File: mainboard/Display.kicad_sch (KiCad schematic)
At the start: 4 parts, among them X1401 DISPLAY

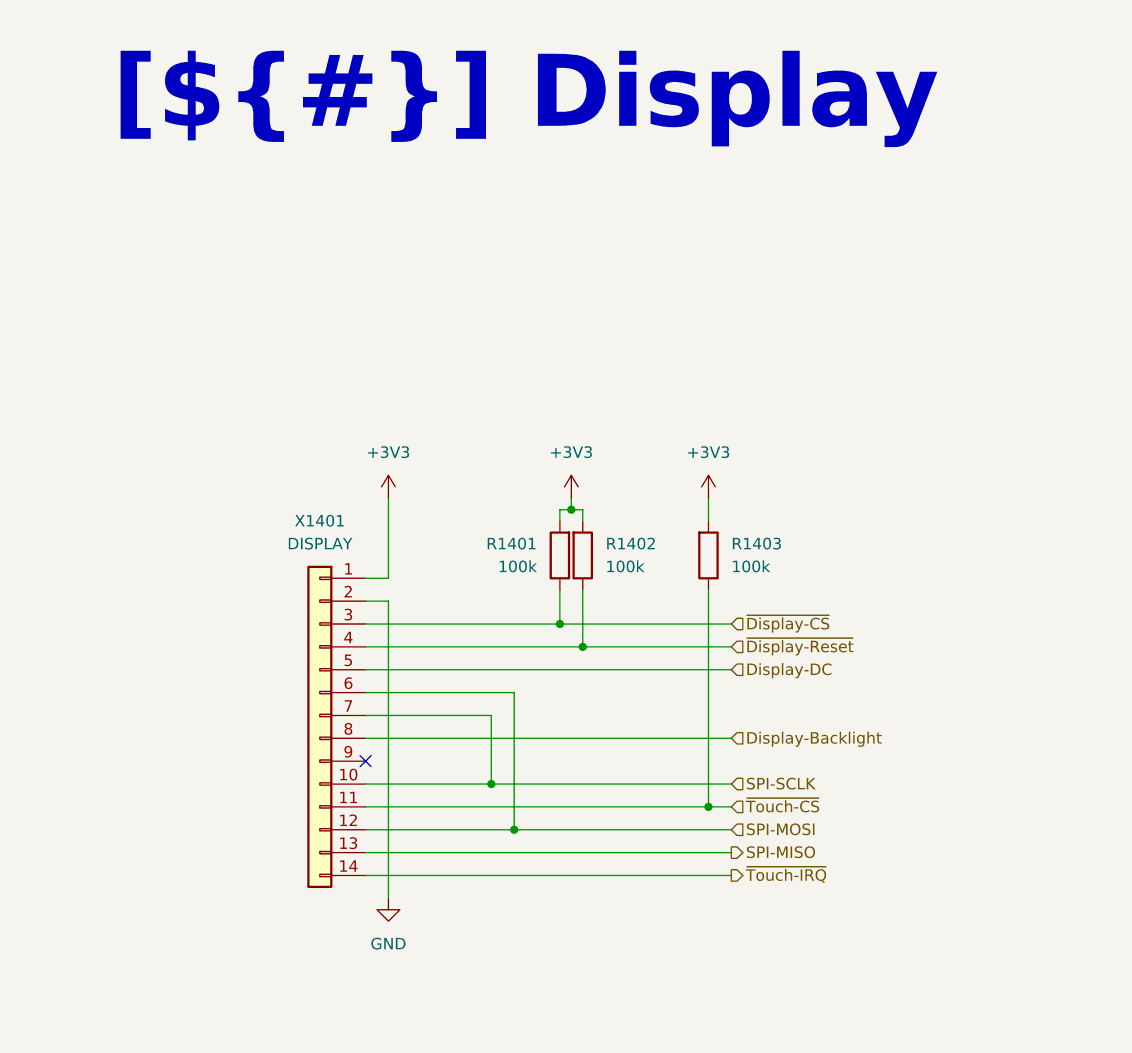
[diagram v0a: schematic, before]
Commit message: Continue routing, add flash LEDs for the RGB camera, add PWM controller for the Display Backlight and the flash LEDs, add Polyfuse for the battery
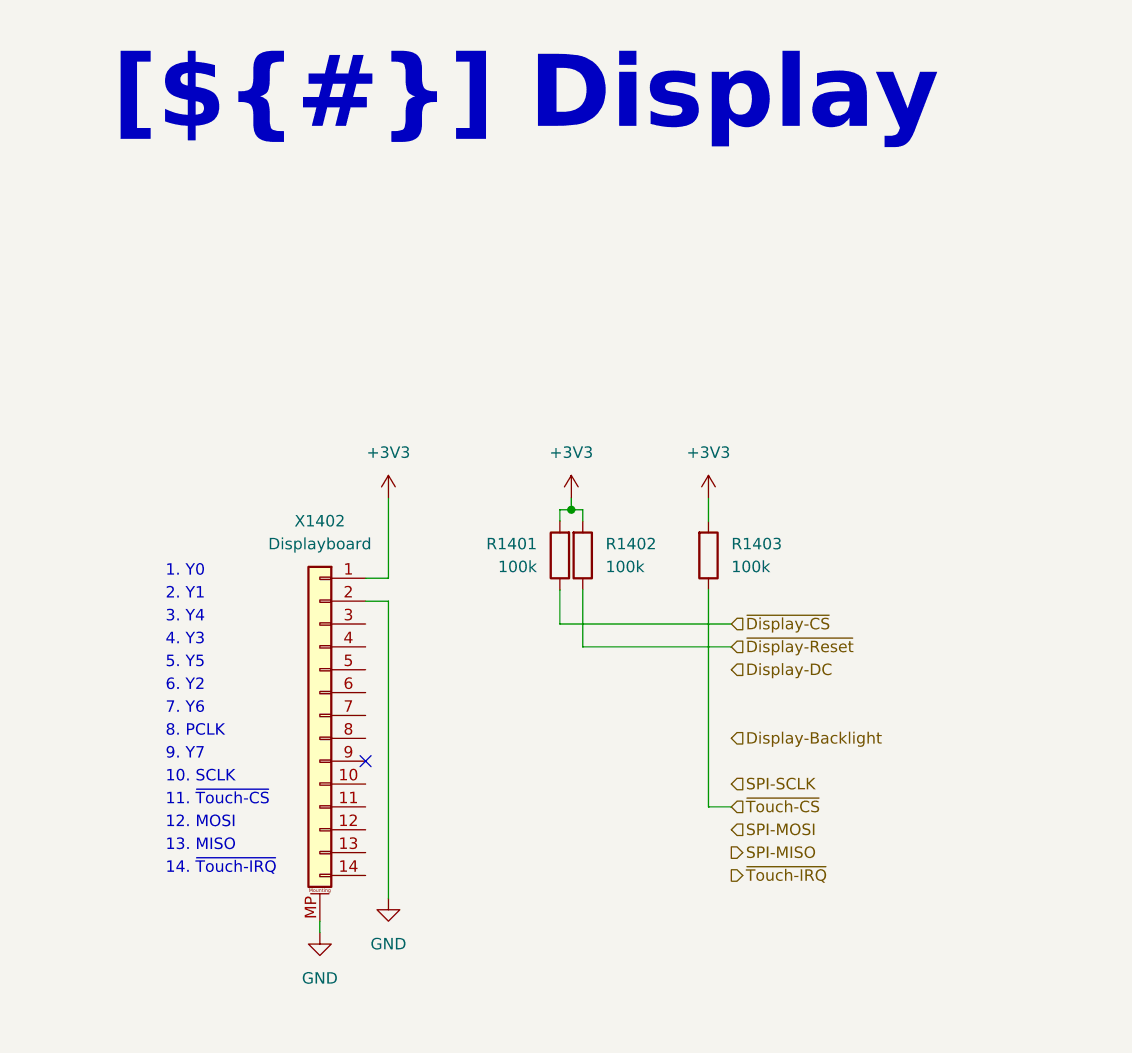
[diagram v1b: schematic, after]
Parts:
- removed X1401: DISPLAY, Connector_PinSocket_2.54mm:PinSocket_1x14_P2.54mm_Vertical, symbol Connector_Generic:Conn_01x14
- added X1402: Displayboard, Connector_FFC-FPC:Amphenol_F32R-1A7x1-11014_1x14-1MP_P0.5mm_Horizontal, symbol Connector_Generic_MountingPin:Conn_01x14_MountingPin
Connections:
- net +3V3: now also X1402.1 (Pin_1)
- net GND: now also X1402.2 (Pin_2), X1402.MP (MountPin)
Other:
- note added: "1. Y0"
- note added: "10. SCLK"
- note added: "11. ~{Touch-CS}"
- note added: "12. MOSI"
- note added: "13. MISO"
- note added: "14. ~{Touch-IRQ}"
- note added: "2. Y1"
- note added: "3. Y4"
- note added: "4. Y3"
- note added: "5. Y5"
- note added: "6. Y2"
- note added: "7. Y6"
- note added: "8. PCLK"
- note added: "9. Y7"

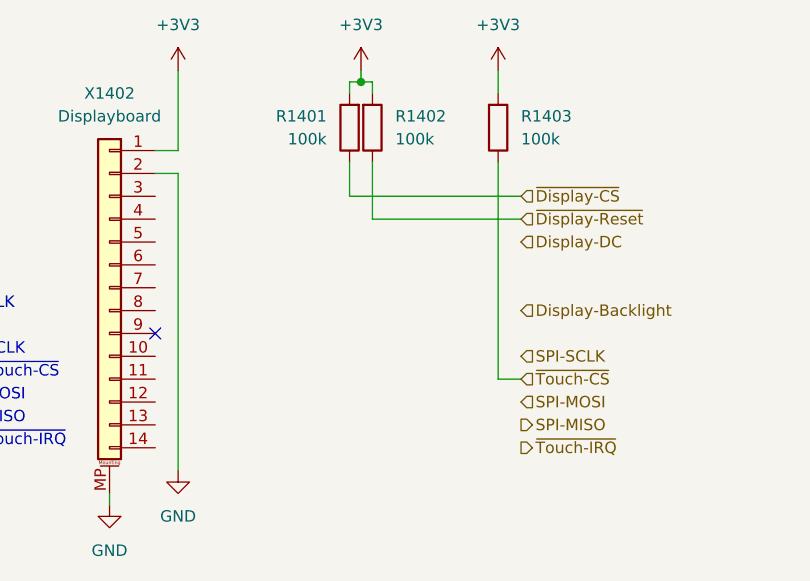
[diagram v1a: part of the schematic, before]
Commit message: New position for display connector
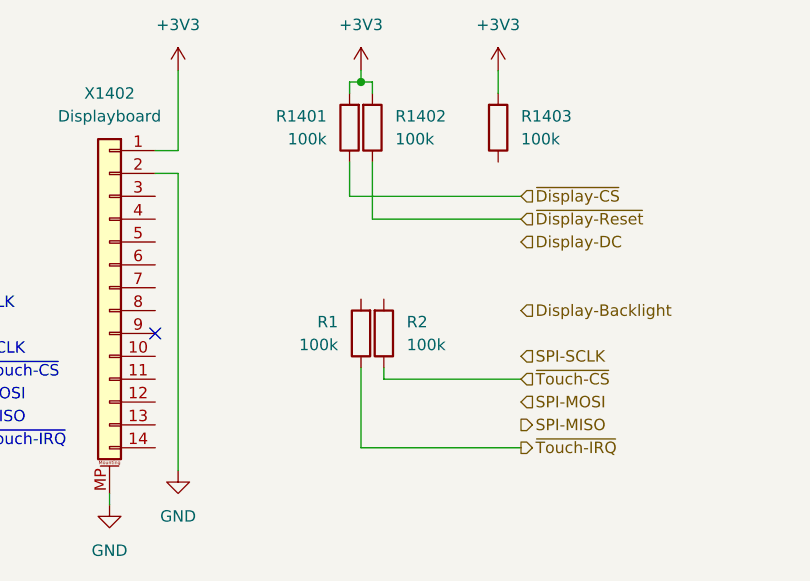
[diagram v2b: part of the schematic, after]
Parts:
- added R1, R2: 100k, Resistor_SMD:R_0603_1608Metric, symbol Device:R
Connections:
- net ~{Touch-CS}: now also R2.1; no longer R1403.1
- net ~{Touch-IRQ}: now also R1.1
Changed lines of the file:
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@@
+	(wire
+		(pts
+			(xy 156.21 99.06) (xy 156.21 97.79)
+		)
+		(stroke
+			(width 0)
+			(type default)
+		)
+	)
 	(wire
 		(pts
@@
 	(wire
 		(pts
+			(xy 171.45 106.68) (xy 153.67 106.68)
+		)
+		(stroke
+			(width 0)
+			(type default)
+		)
+	)
+	(wire
+		(pts
 			(xy 154.94 81.28) (xy 171.45 81.28)
 		)
@@
 	(wire
 		(pts
-			(xy 168.91 99.06) (xy 171.45 99.06)
+			(xy 153.67 106.68) (xy 153.67 97.79)
+		)
+		(stroke
+			(width 0)
+			(type default)
+		)
+	)
+	(wire
+		(pts
+			(xy 156.21 99.06) (xy 171.45 99.06)
 		)
 		(stroke
@@
 		(pts
 			(xy 133.35 76.2) (xy 133.35 109.22)
-		)
-		(stroke
-			(width 0)
-			(type default)
-		)
-	)
-	(wire
-		(pts
-			(xy 168.91 74.93) (xy 168.91 99.06)
 		)
 		(stroke
@@
 	)
 	(symbol
+		(lib_id "Device:R")
+		(at 153.67 93.98 180)
+		(unit 1)
+		(exclude_from_sim no)
+		(in_bom yes)
+		(on_board yes)
+		(dnp no)
+		(property "Reference" "R1"
+			(at 151.13 92.7099 0)
+			(effects
+				(font
+					(size 1.27 1.27)
+				)
+				(justify left)
+			)
+		)
+		(property "Value" "100k"
+			(at 151.13 95.2499 0)
+			(effects
+				(font
+					(size 1.27 1.27)
+				)
+				(justify left)
+			)
+		)
+		(property "Footprint" "Resistor_SMD:R_0603_1608Metric"
+			(at 155.448 93.98 90)
+			(effects
+				(font
+					(size 1.27 1.27)
+				)
+				(hide yes)
+			)
+		)
+		(property "Datasheet" "https://www.mouser.de/datasheet/2/54/cr-1858361.pdf"
+			(at 153.67 93.98 0)
+			(effects
+				(font
+					(size 1.27 1.27)
+				)
+				(hide yes)
+			)
+		)
+		(property "Description" "Resistor"
+			(at 153.67 93.98 0)
+			(effects
+				(font
+					(size 1.27 1.27)
+				)
+				(hide yes)
+			)
+		)
+		(property "CONFIG" ""
+			(at 153.67 93.98 0)
+			(effects
+				(font
+					(size 1.27 1.27)
+				)
+				(hide yes)
+			)
+		)
+		(property "manf" "Bourns"
+			(at 153.67 93.98 0)
+			(effects
+				(font
+					(size 1.27 1.27)
+				)
+				(hide yes)
+			)
+		)
+		(property "manf#" "CR0603-JW-104ELF"
+			(at 153.67 93.98 0)
+			(effects
+				(font
+					(size 1.27 1.27)
+				)
+				(hide yes)
+			)
+		)
+		(property "mouser#" "652-CR0603-JW-104ELF"
+			(at 153.67 93.98 0)
+			(effects
+				(font
+					(size 1.27 1.27)
+				)
+				(hide yes)
+			)
+		)
+		(pin "1"
+		)
+		(pin "2"
+		)
+		(instances
+			(project "Mainboard"
+				(path "/d5742f03-3b1a-42e5-a384-018bd4b919aa/c5103ceb-5325-4a84-a025-9638a412984e/87ec52b1-2e4e-4bae-bd8b-72c5c03421b9"
+					(reference "R1")
+					(unit 1)
+				)
+			)
+		)
+	)
+	(symbol
 		(lib_id "power:GND")
 		(at 125.73 113.03 0)
@@
 					(unit 1)
 				)
+			)
+		)
+	)
+	(symbol
+		(lib_id "Device:R")
+		(at 156.21 93.98 0)
+		(mirror x)
+		(unit 1)
+		(exclude_from_sim no)
+		(in_bom yes)
+		(on_board yes)
+		(dnp no)
+		(fields_autoplaced yes)
+		(property "Reference" "R2"
+			(at 158.75 92.7099 0)
+			(effects
+				(font
+					(size 1.27 1.27)
+				)
+				(justify left)
+			)
+		)
+		(property "Value" "100k"
+			(at 158.75 95.2499 0)
+			(effects
+				(font
+					(size 1.27 1.27)
+				)
+				(justify left)
+			)
+		)
+		(property "Footprint" "Resistor_SMD:R_0603_1608Metric"
+			(at 154.432 93.98 90)
+			(effects
+				(font
+					(size 1.27 1.27)
+				)
+				(hide yes)
+			)
+		)
+		(property "Datasheet" "https://www.mouser.de/datasheet/2/54/cr-1858361.pdf"
+			(at 156.21 93.98 0)
+			(effects
+				(font
+					(size 1.27 1.27)
+				)
+				(hide yes)
+			)
+		)
+		(property "Description" "Resistor"
+			(at 156.21 93.98 0)
+			(effects
+				(font
+					(size 1.27 1.27)
+				)
+				(hide yes)
+			)
+		)
+		(property "CONFIG" ""
+			(at 156.21 93.98 0)
+			(effects
+				(font
+					(size 1.27 1.27)
+				)
+				(hide yes)
+			)
+		)
+		(property "manf" "Bourns"
+			(at 156.21 93.98 0)
+			(effects
+				(font
+					(size 1.27 1.27)
+				)
+				(hide yes)
+			)
+		)
+		(property "manf#" "CR0603-JW-104ELF"
+			(at 156.21 93.98 0)
+			(effects
+				(font
+					(size 1.27 1.27)
+				)
+				(hide yes)
+			)
+		)
+		(property "mouser#" "652-CR0603-JW-104ELF"
+			(at 156.21 93.98 0)
+			(effects
+				(font
+					(size 1.27 1.27)
+				)
+				(hide yes)
+			)
+		)
+		(pin "1"
+		)
+		(pin "2"
+		)
+		(instances
+			(project "Mainboard"
+				(path "/d5742f03-3b1a-42e5-a384-018bd4b919aa/c5103ceb-5325-4a84-a025-9638a412984e/87ec52b1-2e4e-4bae-bd8b-72c5c03421b9"
+					(reference "R2")
+					(unit 1)
+				)

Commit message: Layout complete
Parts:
- renumbered R1403 to R1401, R1401 to R1402, R1402 to R1403, R2 to R1404, R1 to R1405, X1402 to X1401
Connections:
- net ~{Touch-CS} is gone; now on net ~{Display-Expander-Int}: R1404.1
- net +3V3: now also R1404.2, R1405.2, X1401.14 (Pin_14); no longer X1401.1 (Pin_1)
- net Display-Backlight: now also X1401.1 (Pin_1)
- net Display-DC: now also X1401.5 (Pin_5)
- net GND: now also X1401.13 (Pin_13); no longer X1401.2 (Pin_2)
- net SPI-MISO: now also X1401.2 (Pin_2)
- net SPI-MOSI: now also X1401.3 (Pin_3)
- net SPI-SCLK: now also X1401.6 (Pin_6)
- net ~{Display-CS}: now also R1401.1, X1401.4 (Pin_4); no longer R1402.1
- net ~{Display-Reset}: now also R1405.1, X1401.7 (Pin_7); no longer R1403.1
- net ~{Touch-IRQ}: now also R1403.1, X1401.11 (Pin_11); no longer R1405.1
- net I2C-SDA: now reaches X1401.10 (Pin_10)
- net ~{Touch-Reset}: now reaches X1401.12 (Pin_12)
- net ~{Touch-Reset}: now also R1402.1
- net ~{Display-Expander-Int}: now reaches X1401.8 (Pin_8)
- net I2C-SCL: now reaches X1401.9 (Pin_9)
- no-connect marks 1 -> 0
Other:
- note added: "1. +3V3"
- note added: "10. Display-DC"
- note added: "11. ~{Display-CS}"
- note added: "12. SPI-MOSI"
- note added: "13. SPI-MISO"
- note added: "14. Display-Backlight"
- note added: "2. GND"
- note added: "3. ~{Touch-Reset}"
- note added: "4. ~{Touch-IRQ}"
- note added: "5. SDA"
- note added: "6. SCL"
- note added: "7. ~{Expander-Int}"
- note added: "8. ~{Display-Reset}"
- note added: "9. SPI-SCLK"
- note removed: "1. Y0"
- note removed: "10. SCLK"
- note removed: "11. ~{Touch-CS}"
- note removed: "12. MOSI"
- note removed: "13. MISO"
- note removed: "14. ~{Touch-IRQ}"
- note removed: "2. Y1"
- note removed: "3. Y4"
- note removed: "4. Y3"
- note removed: "5. Y5"
- note removed: "6. Y2"
- note removed: "7. Y6"
- note removed: "8. PCLK"
- note removed: "9. Y7"
- moved on the sheet: R1401, R1402, R1403, R1404, R1405

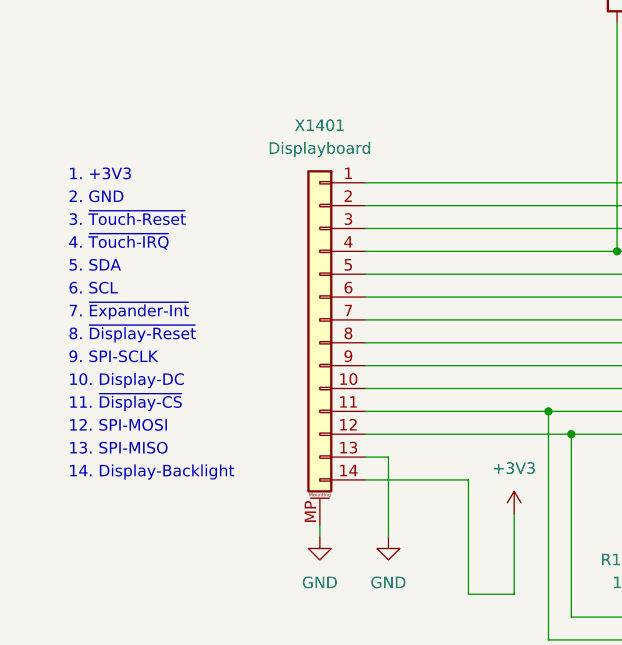
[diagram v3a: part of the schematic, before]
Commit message: Changed: Fix different minor assembly ToDos
Signed-off-by: Daniel Kampert <DanielKampert@kampis-elektroecke.de>
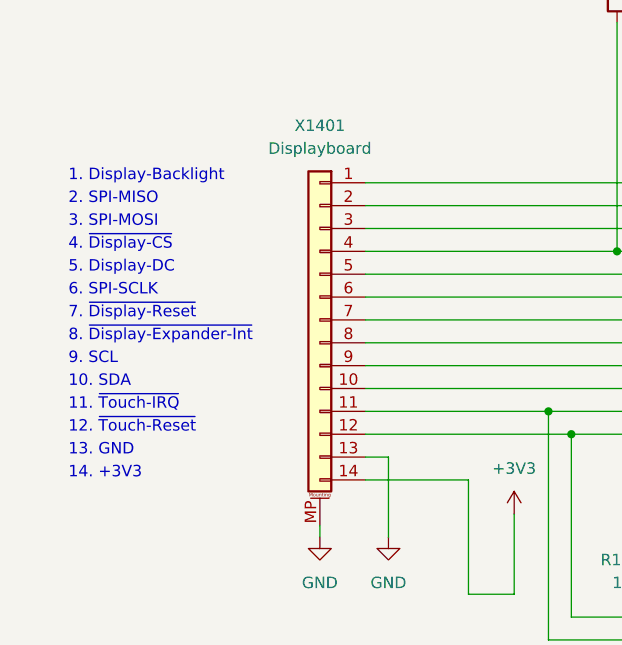
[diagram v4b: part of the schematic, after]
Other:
- note added: "1. Display-Backlight"
- note added: "10. SDA"
- note added: "11. ~{Touch-IRQ}"
- note added: "12. ~{Touch-Reset}"
- note added: "13. GND"
- note added: "14. +3V3"
- note added: "2. SPI-MISO"
- note added: "3. SPI-MOSI"
- note added: "4. ~{Display-CS}"
- note added: "5. Display-DC"
- note added: "6. SPI-SCLK"
- note added: "7. ~{Display-Reset}"
- note added: "8. ~{Display-Expander-Int}"
- note added: "9. SCL"
- note removed: "1. +3V3"
- note removed: "10. Display-DC"
- note removed: "11. ~{Display-CS}"
- note removed: "12. SPI-MOSI"
- note removed: "13. SPI-MISO"
- note removed: "14. Display-Backlight"
- note removed: "2. GND"
- note removed: "3. ~{Touch-Reset}"
- note removed: "4. ~{Touch-IRQ}"
- note removed: "5. SDA"
- note removed: "6. SCL"
- note removed: "7. ~{Expander-Int}"
- note removed: "8. ~{Display-Reset}"
- note removed: "9. SPI-SCLK"
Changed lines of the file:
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@@
 		(company "${COMPANY}")
 	)
-	(text "6. SCL"
+	(text "6. SPI-SCLK"
 		(exclude_from_sim no)
 		(at 97.79 86.36 0)
@@
 		)
 	)
-	(text "10. Display-DC"
+	(text "10. SDA"
 		(exclude_from_sim no)
 		(at 97.79 96.52 0)
@@
 		)
 	)
-	(text "12. SPI-MOSI"
+	(text "12. ~{Touch-Reset}"
 		(exclude_from_sim no)
 		(at 97.79 101.6 0)
@@
 		)
 	)
-	(text "7. ~{Expander-Int}"
+	(text "7. ~{Display-Reset}"
 		(exclude_from_sim no)
 		(at 97.79 88.9 0)
@@
 		)
 	)
-	(text "13. SPI-MISO"
+	(text "13. GND"
 		(exclude_from_sim no)
 		(at 97.79 104.14 0)
@@
 		)
 	)
-	(text "1. +3V3"
+	(text "1. Display-Backlight"
 		(exclude_from_sim no)
 		(at 97.79 73.66 0)
@@
 		)
 	)
-	(text "4. ~{Touch-IRQ}"
+	(text "4. ~{Display-CS}"
 		(exclude_from_sim no)
 		(at 97.79 81.28 0)
@@
 		)
 	)
-	(text "5. SDA"
+	(text "5. Display-DC"
 		(exclude_from_sim no)
 		(at 97.79 83.82 0)
@@
 		)
 	)
-	(text "11. ~{Display-CS}"
+	(text "11. ~{Touch-IRQ}"
 		(exclude_from_sim no)
 		(at 97.79 99.06 0)
@@
 		)
 	)
-	(text "3. ~{Touch-Reset}"
+	(text "3. SPI-MOSI"
 		(exclude_from_sim no)
 		(at 97.79 78.74 0)
@@
 		)
 	)
-	(text "8. ~{Display-Reset}"
+	(text "8. ~{Display-Expander-Int}"
 		(exclude_from_sim no)
 		(at 97.79 91.44 0)
@@
 		)
 	)
-	(text "14. Display-Backlight"
+	(text "14. +3V3"
 		(exclude_from_sim no)
 		(at 97.79 106.68 0)
@@
 		)
 	)
-	(text "2. GND"
+	(text "2. SPI-MISO"
 		(exclude_from_sim no)
 		(at 97.79 76.2 0)
@@
 		)
 	)
-	(text "9. SPI-SCLK"
+	(text "9. SCL"
 		(exclude_from_sim no)
 		(at 97.79 93.98 0)
